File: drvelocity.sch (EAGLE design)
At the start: 8 parts, among them U1 DRV8704

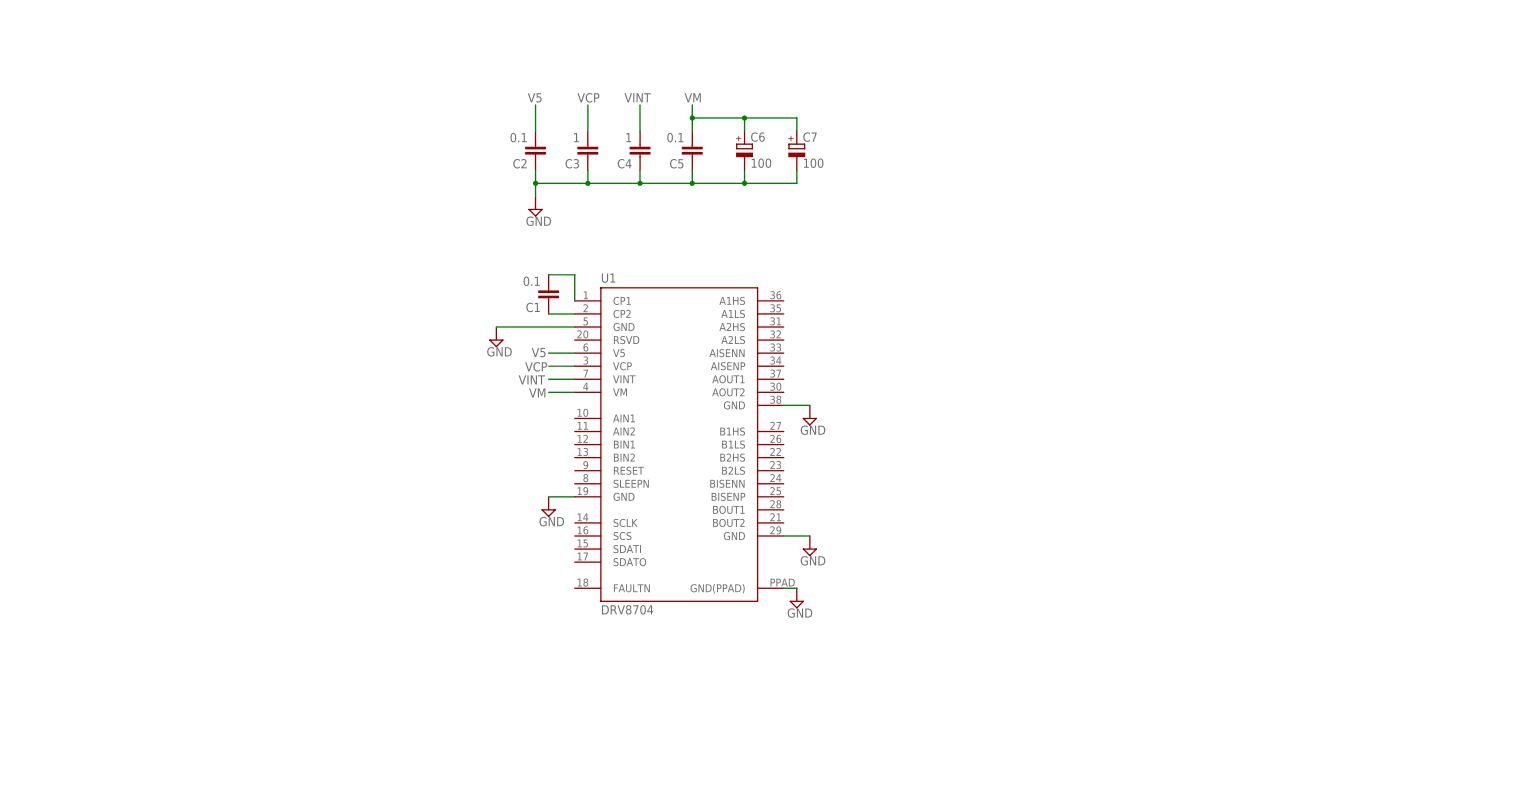
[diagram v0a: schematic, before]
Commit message: Lay out H-Bridge
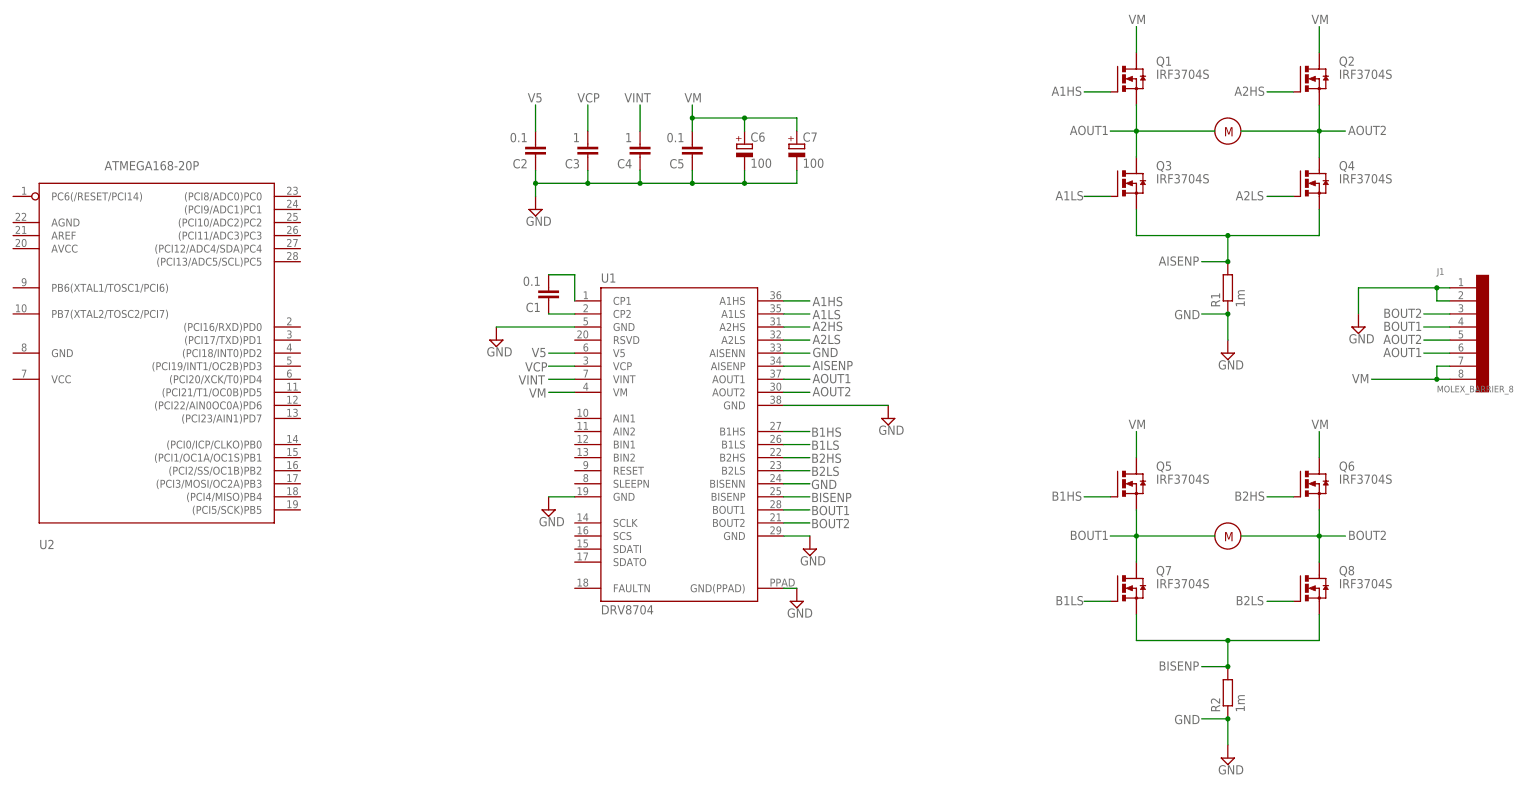
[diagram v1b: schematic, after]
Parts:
- added J1: MOLEX_BARRIER_8, Molex Barrier Terminal:MOLEX_BARRIER_8
- added Q1, Q2, Q3, Q4, Q5, Q6, Q7, Q8: IRF3704S, transistor-power:IRF3704S
- added R1, R2: 1m, resistor:R-EU_R4527
- added U2: ATMEGA168-20P, adafruit:ATMEGA168-20P
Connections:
- new net A1HS: Q1.G, U1.A1HS
- new net A1LS: Q3.G, U1.A1LS
- new net A2HS: Q2.G, U1.A2HS
- new net A2LS: Q4.G, U1.A2LS
- new net AISENP: Q3.S, Q4.S, R1.2, U1.AISENP
- new net AOUT1: J1.@6, Q1.S, Q3.D, U1.AOUT1
- new net AOUT2: J1.@5, Q2.S, Q4.D, U1.AOUT2
- new net B1HS: Q5.G, U1.B1HS
- new net B1LS: Q7.G, U1.B1LS
- new net B2HS: Q6.G, U1.B2HS
- new net B2LS: Q8.G, U1.B2LS
- new net BISENP: Q7.S, Q8.S, R2.2, U1.BISENP
- new net BOUT1: J1.@4, Q5.S, Q7.D, U1.BOUT1
- new net BOUT2: J1.@3, Q6.S, Q8.D, U1.BOUT2
- net GND: now also J1.@1, J1.@2, R1.1, R2.1, U1.AISENN, U1.BISENN
- net VM: now also J1.@7, J1.@8, Q1.D, Q2.D, Q5.D, Q6.D
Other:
- note added: "M"
